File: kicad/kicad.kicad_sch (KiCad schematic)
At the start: 56 parts, among them J1 Conn_01x16_Pin, K0 !,,,,,,1, K1 ",,,,,,2, K10 *,,,,,,:, K11 =,,,,,,-, K12 Break, K13 Up, K14 Q, K15 W, K16 E, K17 R, K18 T, K19 Y, K2 #,,,,,,3, K20 U, K21 I, K22 O, K23 P, K24 @, K25 Left, K26 Right, K27 Down, K28 A, K29 S, K3 $,,,,,,4, K30 D, K31 F, K32 G, K33 H, K34 J, K35 K, K36 L, K37 +,,,,,,;, K38 ENTER, K39 CLEAR, K4 %,,,,,,5, K40 SHIFT, K41 Z, K42 X, K43 C, K44 V, K45 B, K46 N, K47 M, K48 <,,,,,,,, K49 >,,,,,,., K5 &,,,,,,6, K50 ?,,,,,,/, K51 SHIFT, K52 Blank, K6 ',,,,,,7, K7 (,,,,,,8, K8 ),,,,,,9, K9 0

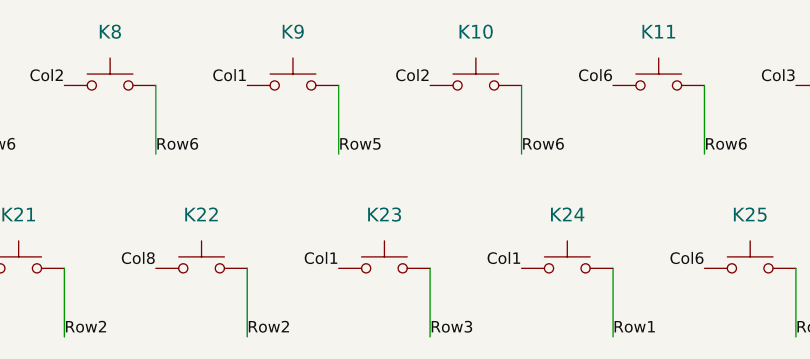
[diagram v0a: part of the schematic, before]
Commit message: Fix asterisk key
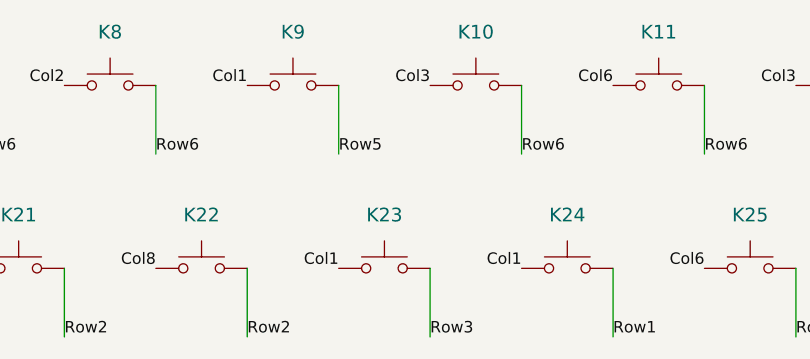
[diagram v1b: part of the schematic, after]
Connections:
- net Col2: no longer K10.1
- net Col3: now also K10.1
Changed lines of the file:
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@@
 		)
 	)
-	(label "Col2"
+	(label "Col3"
 		(at 248.92 26.67 180)
 		(fields_autoplaced yes)

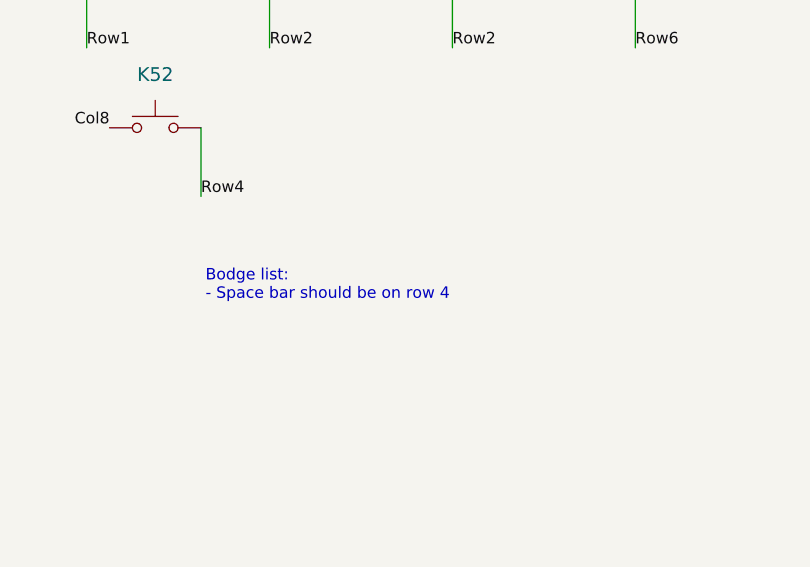
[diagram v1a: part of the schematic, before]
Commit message: Produce v2 prototype gerbers for nickle241
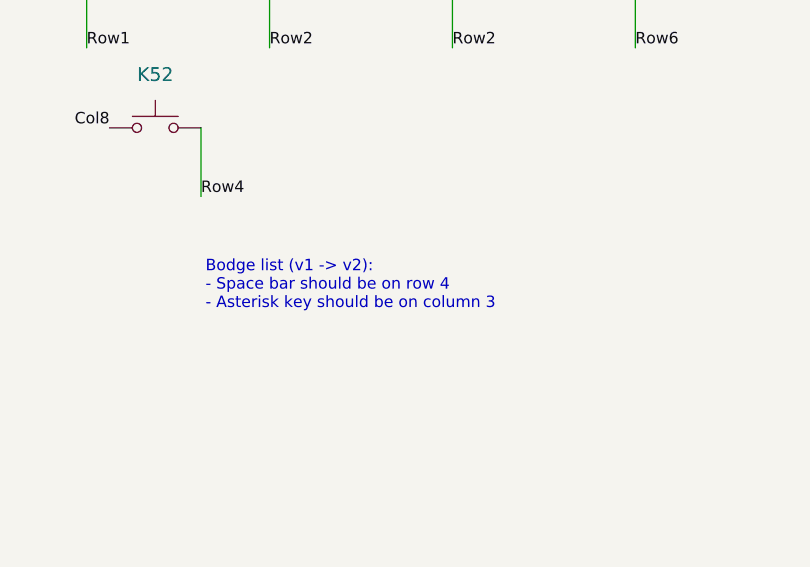
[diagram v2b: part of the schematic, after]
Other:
- note added: "Bodge list (v1 -> v2): - Space bar should be on row 4 - Asterisk key should be on column 3"
- note removed: "Bodge list: - Space bar should be on row 4"
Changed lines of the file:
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@@
 		)
 	)
-	(text "Bodge list:\n- Space bar should be on row 4"
+	(text "Bodge list (v1 -> v2):\n- Space bar should be on row 4\n- Asterisk key should be on column 3"
 		(exclude_from_sim no)
 		(at 175.768 116.586 0)
